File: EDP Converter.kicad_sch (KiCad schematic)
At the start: 64 parts, among them J1 47272-0001, J2 Conn_01x22_Socket, J3 Conn_02x20_Odd_Even, U1 SN65DSI86IPAPRQ1, U2 MCP1700x-180xxTT, U3 MCP1700x-120xxTT, U4 TXB0104RGY, U5 74LVC1G07

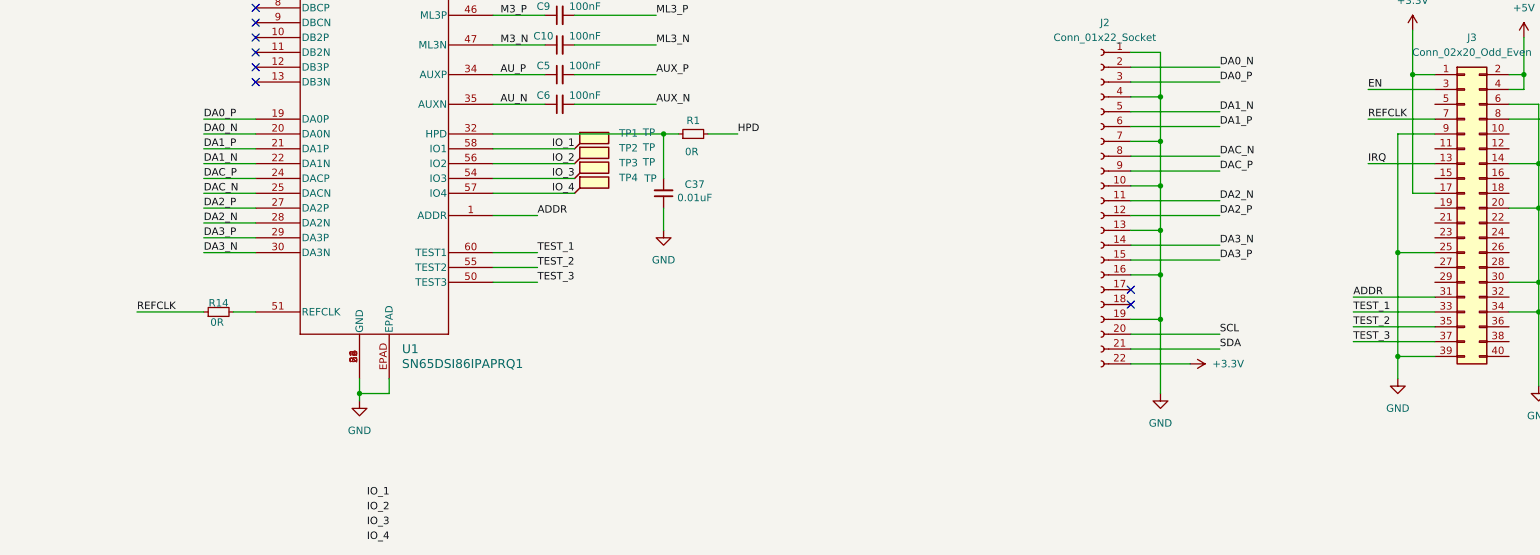
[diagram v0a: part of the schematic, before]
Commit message: added the v1.1 which few modifications
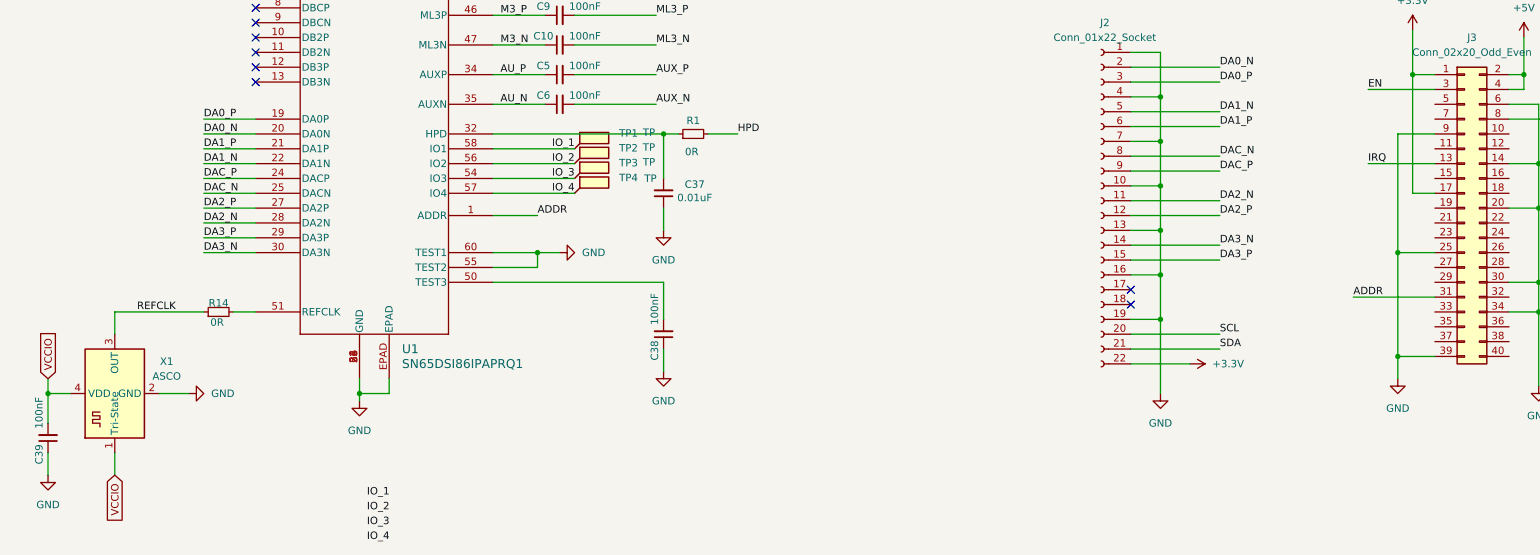
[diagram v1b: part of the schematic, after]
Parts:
- added C38, C39: 100nF, Capacitor_SMD:C_0402_1005Metric, symbol Device:C_Small
- added X1: ASCO, Oscillator:Oscillator_SMD_Abracon_ASCO-4Pin_1.6x1.2mm, symbol Oscillator:ASCO
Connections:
- net GND: now also U1.55 (TEST2), U1.60 (TEST1), C38.1, C39.1, X1.2 (GND)
- net REFCLK: now also X1.3 (OUT); no longer J3.7 (Pin_7)
- net VCCIO: now also C39.2, X1.1 (Tri-State), X1.4 (VDD)
- net TEST_1: no longer names the net of J3.33 (Pin_33)
- net TEST_1: no longer U1.60 (TEST1)
- net TEST_2: no longer names the net of J3.35 (Pin_35)
- net TEST_2: no longer U1.55 (TEST2)
- net TEST_3: no longer names the net of U1.50 (TEST3)
- net TEST_3: now also C38.2; no longer J3.37 (Pin_37)
